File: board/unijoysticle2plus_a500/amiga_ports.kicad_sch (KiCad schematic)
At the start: 18 parts, among them J2 PORT JOY #1, J3 PORT JOY #2, SW3 USER1, SW4 USER2, U4 74HC05, U5 74HC05, U6 74HC05

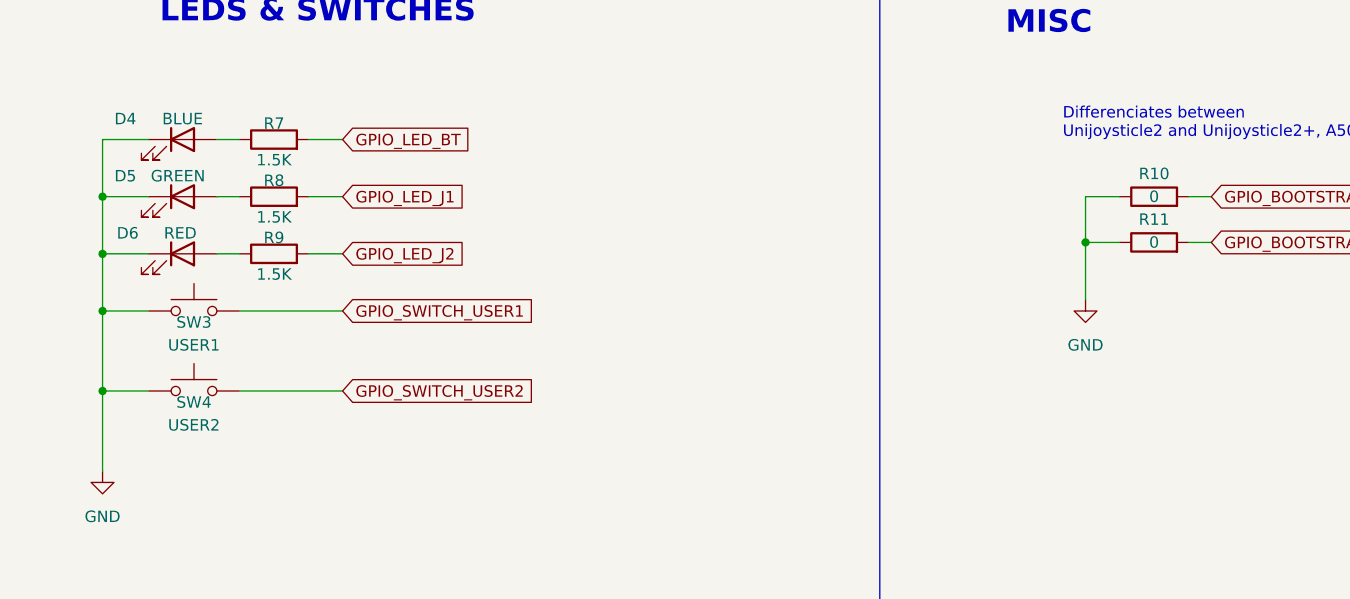
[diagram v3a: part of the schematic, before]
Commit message: Uni 2+ A500: many little changes
- replace resistor 0 with solder jumper for strapping pins
- move big cap a big down
- improved routing
- move vias outside pads
... and more
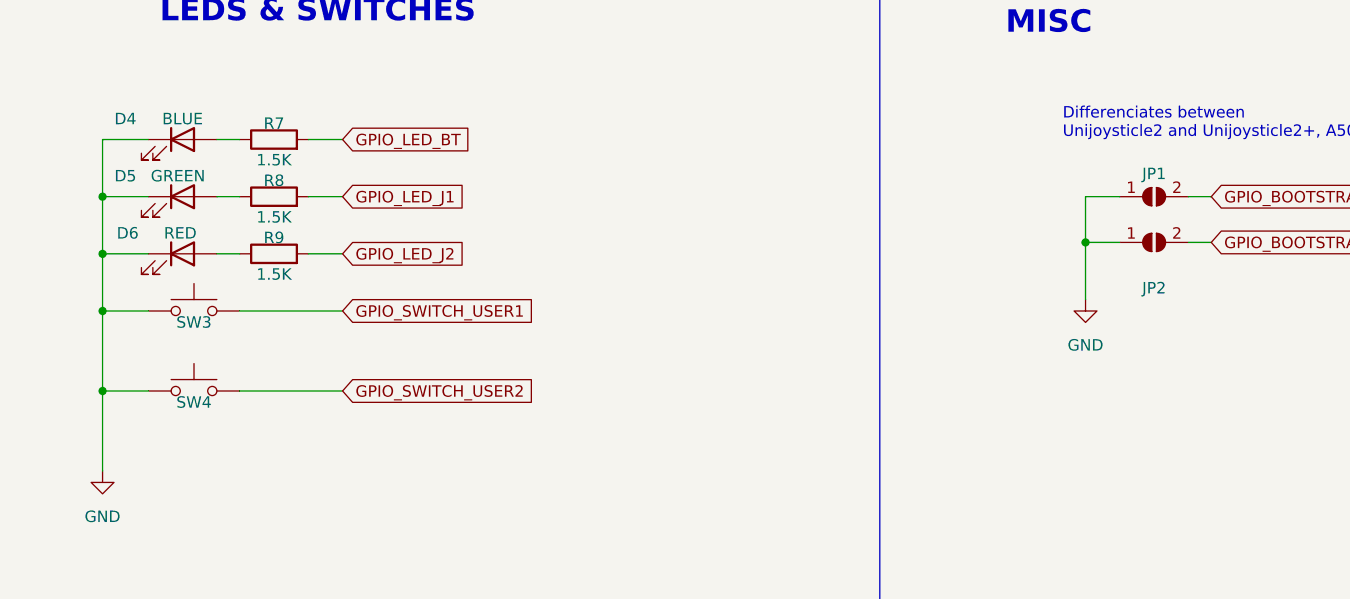
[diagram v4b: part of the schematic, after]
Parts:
- removed R10, R11: 0, Resistor_SMD:R_0805_2012Metric_Pad1.20x1.40mm_HandSolder, symbol Device:R
- added JP1, JP2: (no value), symbol Jumper:SolderJumper_2_Open
- SW3: value USER1 -> (none)
- SW4: value USER2 -> (none)
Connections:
- net GND: now also JP1.1 (A), JP2.1 (A)
- net GPIO_BOOTSTRAP_04: now also JP1.2 (B)
- net GPIO_BOOTSTRAP_36: now also JP2.2 (B)
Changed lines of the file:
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@@
     (in_bom yes) (on_board yes)
     (property "Reference" "SW3" (id 0) (at 34.29 158.75 0))
-    (property "Value" "USER1" (id 1) (at 34.29 161.29 0))
+    (property "Value" "" (id 1) (at 34.29 161.29 0))
     (property "Footprint" "Button_Switch_THT:SW_Tactile_SPST_Angled_PTS645Vx39-2LFS" (id 2) (at 34.29 152.4 0)
       (effects (font (size 1.27 1.27)) hide)
@@
     (pin "7")
   )
+  (symbol (lib_id "Jumper:SolderJumper_2_Open") (at 140.97 144.78 0) (unit 1)
+    (in_bom yes) (on_board yes)
+    (property "Reference" "JP1" (id 0) (at 140.97 142.24 0))
+    (property "Value" "" (id 1) (at 140.97 147.32 0))
+    (property "Footprint" "" (id 2) (at 140.97 144.78 0)
+      (effects (font (size 1.27 1.27)) hide)
+    )
+    (property "Datasheet" "~" (id 3) (at 140.97 144.78 0)
+      (effects (font (size 1.27 1.27)) hide)
+    )
+    (pin "1")
+    (pin "2")
+  )
   (symbol (lib_id "power:GND") (at 212.09 92.71 0) (unit 1)
     (in_bom yes) (on_board yes) (fields_autoplaced)
-    (property "Reference" "#PWR0110" (id 0) (at 212.09 99.06 0)
+    (property "Reference" "#PWR035" (id 0) (at 212.09 99.06 0)
       (effects (font (size 1.27 1.27)) hide)
     )
@@
   (symbol (lib_id "power:+5V") (at 240.03 87.63 0) (unit 1)
     (in_bom yes) (on_board yes) (fields_autoplaced)
-    (property "Reference" "#PWR0107" (id 0) (at 240.03 91.44 0)
+    (property "Reference" "#PWR036" (id 0) (at 240.03 91.44 0)
       (effects (font (size 1.27 1.27)) hide)
     )
@@
     (pin "1")
   )
-  (symbol (lib_id "Device:R") (at 140.97 144.78 90) (unit 1)
-    (in_bom yes) (on_board yes)
-    (property "Reference" "R10" (id 0) (at 140.97 142.24 90))
-    (property "Value" "0" (id 1) (at 140.97 144.78 90))
-    (property "Footprint" "Resistor_SMD:R_0805_2012Metric_Pad1.20x1.40mm_HandSolder" (id 2) (at 140.97 146.558 90)
-      (effects (font (size 1.27 1.27)) hide)
-    )
-    (property "Datasheet" "~" (id 3) (at 140.97 144.78 0)
-      (effects (font (size 1.27 1.27)) hide)
-    )
-    (pin "1")
-    (pin "2")
-  )
   (symbol (lib_id "power:+5V") (at 43.18 78.74 0) (unit 1)
     (in_bom yes) (on_board yes) (fields_autoplaced)
-    (property "Reference" "#PWR0102" (id 0) (at 43.18 82.55 0)
+    (property "Reference" "#PWR027" (id 0) (at 43.18 82.55 0)
       (effects (font (size 1.27 1.27)) hide)
     )
@@
     (pin "1")
   )
-  (symbol (lib_id "Device:R") (at 140.97 149.86 90) (unit 1)
-    (in_bom yes) (on_board yes)
-    (property "Reference" "R11" (id 0) (at 140.97 147.32 90))
-    (property "Value" "0" (id 1) (at 140.97 149.86 90))
-    (property "Footprint" "Resistor_SMD:R_0805_2012Metric_Pad1.20x1.40mm_HandSolder" (id 2) (at 140.97 151.638 90)
-      (effects (font (size 1.27 1.27)) hide)
-    )
-    (property "Datasheet" "~" (id 3) (at 140.97 149.86 0)
-      (effects (font (size 1.27 1.27)) hide)
-    )
-    (pin "1")
-    (pin "2")
-  )
   (symbol (lib_id "power:GND") (at 71.12 67.31 0) (unit 1)
     (in_bom yes) (on_board yes) (fields_autoplaced)
-    (property "Reference" "#PWR0101" (id 0) (at 71.12 73.66 0)
+    (property "Reference" "#PWR028" (id 0) (at 71.12 73.66 0)
       (effects (font (size 1.27 1.27)) hide)
     )
@@
     (in_bom yes) (on_board yes)
     (property "Reference" "SW4" (id 0) (at 34.29 167.64 0))
-    (property "Value" "USER2" (id 1) (at 34.29 170.18 0))
+    (property "Value" "" (id 1) (at 34.29 170.18 0))
     (property "Footprint" "Button_Switch_THT:SW_Tactile_SPST_Angled_PTS645Vx39-2LFS" (id 2) (at 34.29 161.29 0)
       (effects (font (size 1.27 1.27)) hide)
@@
   (symbol (lib_id "power:GND") (at 186.69 97.79 0) (unit 1)
     (in_bom yes) (on_board yes) (fields_autoplaced)
-    (property "Reference" "#PWR0109" (id 0) (at 186.69 104.14 0)
+    (property "Reference" "#PWR034" (id 0) (at 186.69 104.14 0)
       (effects (font (size 1.27 1.27)) hide)
     )
@@
   (symbol (lib_id "power:GND") (at 265.43 91.44 0) (unit 1)
     (in_bom yes) (on_board yes) (fields_autoplaced)
-    (property "Reference" "#PWR0108" (id 0) (at 265.43 97.79 0)
+    (property "Reference" "#PWR038" (id 0) (at 265.43 97.79 0)
       (effects (font (size 1.27 1.27)) hide)
     )
@@
   (symbol (lib_id "power:+5V") (at 186.69 87.63 0) (unit 1)
     (in_bom yes) (on_board yes) (fields_autoplaced)
-    (property "Reference" "#PWR0112" (id 0) (at 186.69 91.44 0)
+    (property "Reference" "#PWR033" (id 0) (at 186.69 91.44 0)
       (effects (font (size 1.27 1.27)) hide)
     )
@@
   (symbol (lib_id "power:GND") (at 161.29 91.44 0) (unit 1)
     (in_bom yes) (on_board yes) (fields_autoplaced)
-    (property "Reference" "#PWR0106" (id 0) (at 161.29 97.79 0)
+    (property "Reference" "#PWR032" (id 0) (at 161.29 97.79 0)
       (effects (font (size 1.27 1.27)) hide)
     )
@@
   (symbol (lib_id "power:GND") (at 240.03 96.52 0) (unit 1)
     (in_bom yes) (on_board yes) (fields_autoplaced)
-    (property "Reference" "#PWR0111" (id 0) (at 240.03 102.87 0)
+    (property "Reference" "#PWR037" (id 0) (at 240.03 102.87 0)
       (effects (font (size 1.27 1.27)) hide)
     )
@@
     (pin "1")
   )
+  (symbol (lib_id "Jumper:SolderJumper_2_Open") (at 140.97 149.86 0) (unit 1)
+    (in_bom yes) (on_board yes)
+    (property "Reference" "JP2" (id 0) (at 140.97 154.94 0))
+    (property "Value" "" (id 1) (at 140.97 152.4 0))
+    (property "Footprint" "" (id 2) (at 140.97 149.86 0)
+      (effects (font (size 1.27 1.27)) hide)
+    )
+    (property "Datasheet" "~" (id 3) (at 140.97 149.86 0)
+      (effects (font (size 1.27 1.27)) hide)
+    )
+    (pin "1")
+    (pin "2")
+  )
   (symbol (lib_id "power:GND") (at 133.35 156.21 0) (unit 1)
     (in_bom yes) (on_board yes) (fields_autoplaced)
@@
   (symbol (lib_id "power:+5V") (at 135.89 86.36 0) (unit 1)
     (in_bom yes) (on_board yes) (fields_autoplaced)
-    (property "Reference" "#PWR0113" (id 0) (at 135.89 90.17 0)
+    (property "Reference" "#PWR030" (id 0) (at 135.89 90.17 0)
       (effects (font (size 1.27 1.27)) hide)
     )
@@
   (symbol (lib_id "power:GND") (at 135.89 96.52 0) (unit 1)
     (in_bom yes) (on_board yes) (fields_autoplaced)
-    (property "Reference" "#PWR0105" (id 0) (at 135.89 102.87 0)
+    (property "Reference" "#PWR031" (id 0) (at 135.89 102.87 0)
       (effects (font (size 1.27 1.27)) hide)
     )
@@
   (symbol (lib_id "power:GND") (at 35.56 67.31 0) (unit 1)
     (in_bom yes) (on_board yes) (fields_autoplaced)
-    (property "Reference" "#PWR0103" (id 0) (at 35.56 73.66 0)
+    (property "Reference" "#PWR026" (id 0) (at 35.56 73.66 0)
       (effects (font (size 1.27 1.27)) hide)
     )
@@
   (symbol (lib_id "power:GND") (at 24.13 175.26 0) (unit 1)
     (in_bom yes) (on_board yes) (fields_autoplaced)
-    (property "Reference" "#PWR0104" (id 0) (at 24.13 181.61 0)
-      (effects (font (size 1.27 1.27)) hide)
-    )
+    (property "Reference" "#PWR025" (id 0) (at 24.13 181.61 0)
+      (effects (font (size 1.27 1.27)) hide)
+    )

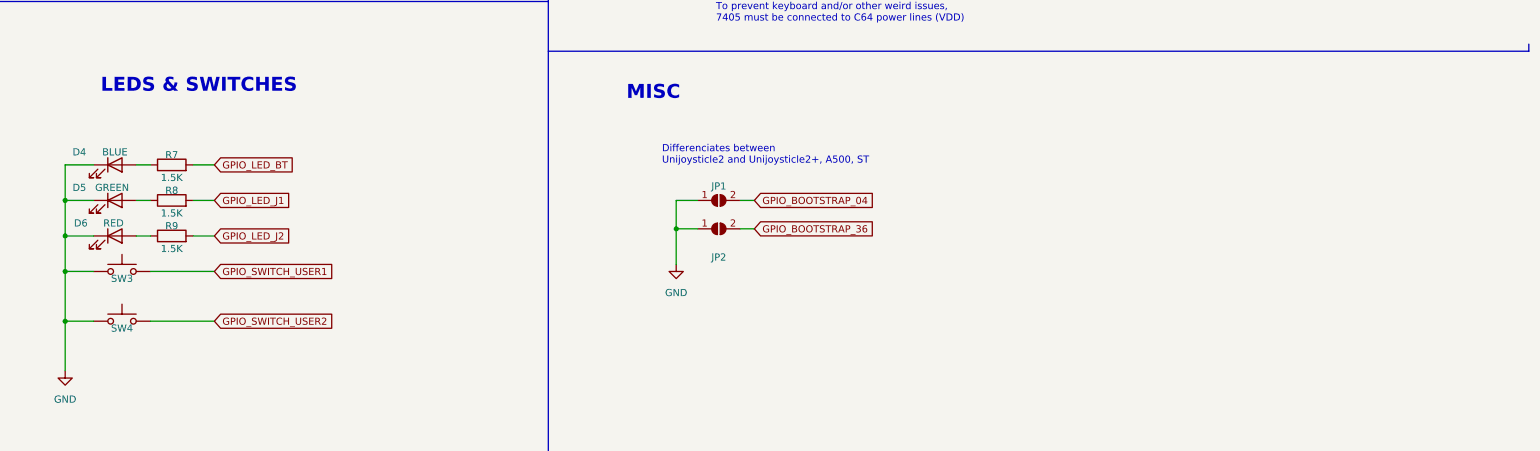
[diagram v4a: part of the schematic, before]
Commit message: A500: Reuse GPIO 15 both as LED and BoardId
Cannot use GPIOs 34~39 for Board ID since in previous models those leds
were floating and those GPIOs don't have pull-up/pull-down resistors.

To GPIO 15 is reused for board id and LEDs.

GPIO 36 and 39 and grounded for future-compatibility.

FIXME:Push buttons won't work. They require a pull-up/pull-down
resistor.
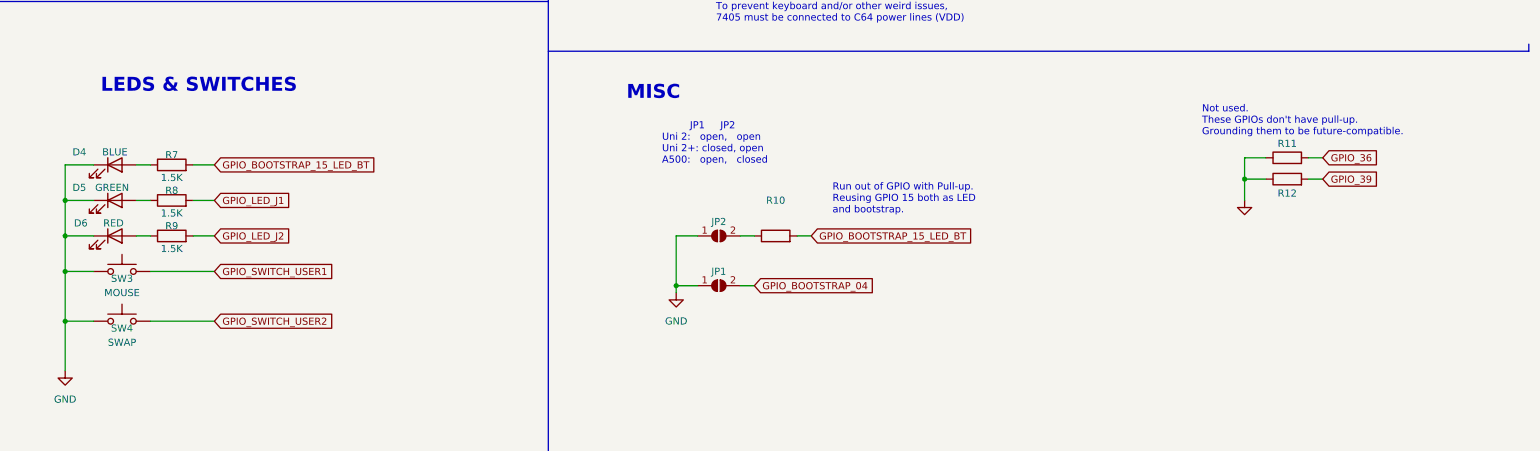
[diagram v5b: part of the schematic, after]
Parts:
- added R10, R11, R12: (no value), symbol Device:R
- JP1, JP2: footprint (none) -> Jumper:SolderJumper-2_P1.3mm_Open_Pad1.0x1.5mm
- SW3: value (none) -> MOUSE
- SW4: value (none) -> SWAP
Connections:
- net GND: now also R11.1, R12.1
- net GPIO_BOOTSTRAP_36: no longer names the net of JP2.2 (B)
- net GPIO_BOOTSTRAP_36: now also R10.1
- net GPIO_LED_BT renamed GPIO_BOOTSTRAP_15_LED_BT
- net GPIO_BOOTSTRAP_15_LED_BT: now also R10.2
- new net GPIO_36: R11.2
- new net GPIO_39: R12.2
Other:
- note added: "JP1 JP2 Uni 2: open, open Uni 2+: closed, open A500: open, closed"
- note added: "Not used. These GPIOs don't have pull-up. Grounding them to be future-compatible."
- note added: "Run out of GPIO with Pull-up. Reusing GPIO 15 both as LED and bootstrap."
- note removed: "Differenciates between Unijoysticle2 and Unijoysticle2+, A500, ST"
- moved on the sheet: JP1, JP2

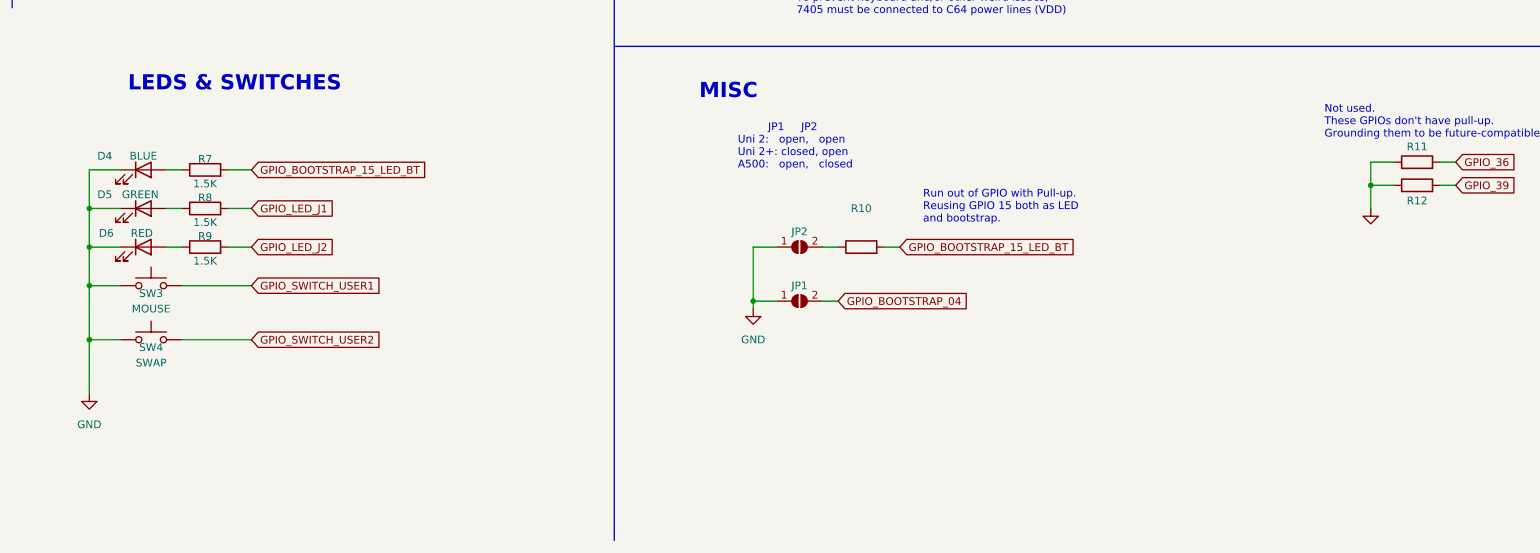
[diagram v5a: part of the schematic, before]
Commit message: a500: add pull-up resistor to push buttons
GPIOs 34~39 don't have internal pull-up.
Add external ones
a#	modified:   unijoysticle2plus_a500.kicad_sch
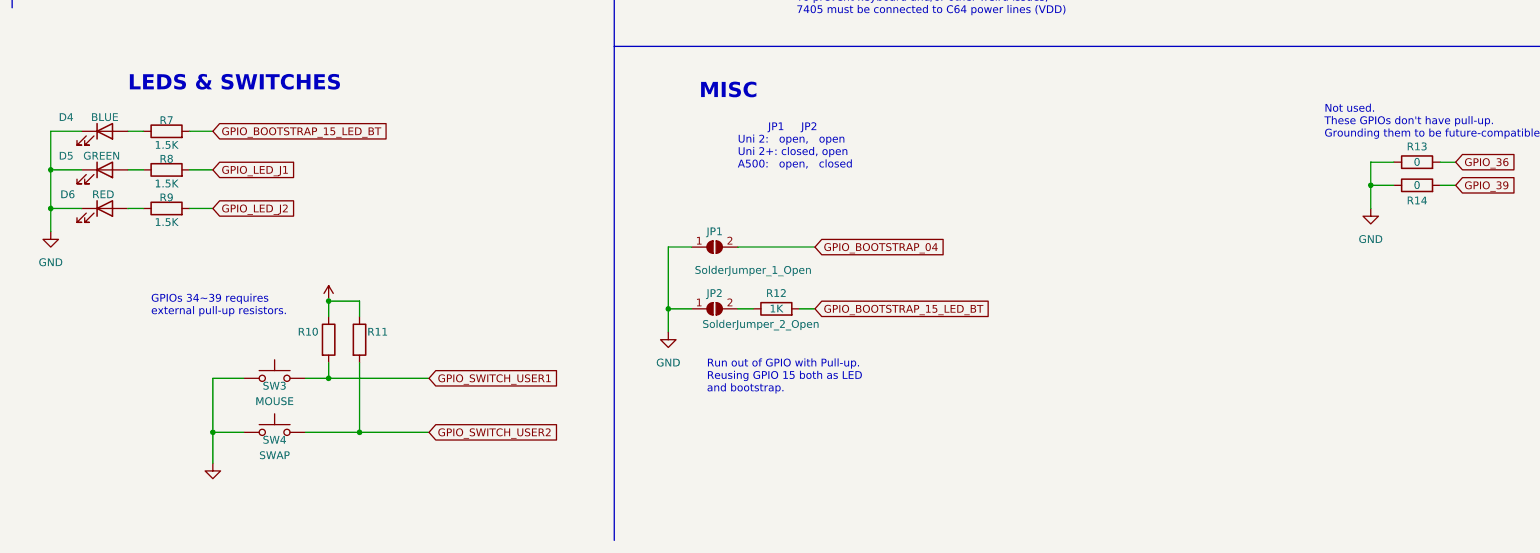
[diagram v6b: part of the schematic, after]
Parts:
- added R10, R11: (no value), symbol Device:R
- JP1: value (none) -> SolderJumper_1_Open
- JP2: value (none) -> SolderJumper_2_Open
- R12: renamed from R10; value (none) -> 1K; footprint (none) -> Resistor_SMD:R_0805_2012Metric_Pad1.20x1.40mm_HandSolder
- R13: renamed from R11; value (none) -> 0; footprint (none) -> Resistor_SMD:R_0805_2012Metric_Pad1.20x1.40mm_HandSolder
- R14: renamed from R12; value (none) -> 0; footprint (none) -> Resistor_SMD:R_0805_2012Metric_Pad1.20x1.40mm_HandSolder
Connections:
- net GPIO_SWITCH_USER1: now also R10.2
- net GPIO_SWITCH_USER2: now also R11.2
- new net +3V3: R10.1, R11.1
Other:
- note added: "GPIOs 34~39 requires external pull-up resistors."
- moved on the sheet: D4, D5, D6, JP1, JP2, R12, R7, R8, R9, SW3, SW4

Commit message: Rename Uni2+ A500 to Uni2 A500
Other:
- title: Unijoysticle 2+ A500 -> Unijoysticle 2 A500
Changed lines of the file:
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@@
   (paper "A4")
   (title_block
-    (title "Unijoysticle 2+ A500")
-    (date "2022-04-20")
+    (title "Unijoysticle 2 A500")
+    (date "2022-04-25")
     (rev "A")
     (company "Retro Moe")
